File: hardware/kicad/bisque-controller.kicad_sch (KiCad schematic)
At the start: 66 parts, among them J1 USB-C, J2 5V_IN, J3 TC1_K, J4 SSR, J5 DISPLAY, J6 NAV_SW, J7 AUX, J8 TC2_K, Q1 AO3400A, Q2 AO3400A, SW1 RESET, SW2 BOOT, U1 ESP32-S3-WROOM-1U-N16R2, U2 AMS1117-3.3, U3 MAX31856MUD+, U4 USBLC6-2SC6, U5 MAX31856MUD+

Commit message: feat(hw): opto-isolate both SSR channels
LTV-817S-TA1-C per channel, indicator LED as a parallel branch (series
would not fit under 3.3V). Both opto and indicator cathodes land on
SSR_EN so the watchdog (task 12) gates the indicator too, never GND
directly. GND pour keepout across the barrier, checked by
check_isolation.py.

Footprint: Package_DIP:SMDIP-4_W9.53mm, not the brief's SO-4_4.4x4.3mm -
REV-B-NOTES.md SS7b measured all four SO-4_4.4x* candidates at a 6.0-6.3mm
pad span against the LTV-817S's ~10.16mm gull-wing lead span; any of them
would land 1.85mm/side inboard of the actual leads. Not using the
_Clearance8mm variant either: that creepage is a mains-crossing
provision, and this barrier is low-voltage on both sides.

Renumbered several of the brief's proposed designators (R15-R19) to
R18/R19/R20/R21/R22 - the brief's originals collided with R14-R17,
already assigned to task 6's MAX31856 input filters.

Also: removed 4 stale ROUTE_ORDER entries in gen_pcb.py that referenced
deleted rev-A SSR nets (would have KeyError'd), and fixed a coincident
schematic-pin bug in gen_sch.py where a new SSR2 resistor and the buzzer
driver's R11 landed on the exact same wire endpoint, silently merging
SSR2_IND_A into the ALARM net.

Co-Authored-By: Claude Opus 5 <noreply@anthropic.com>
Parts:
- removed Q1: AO3400A, Package_TO_SOT_SMD:SOT-23, symbol Transistor_FET:AO3400A
- added J9: SSR2, TerminalBlock_Phoenix:TerminalBlock_Phoenix_MKDS-1,5-2-5.08_1x02_P5.08mm_Horizontal, symbol Connector:Screw_Terminal_01x02
- added LED4: amber, LED_SMD:LED_0805_2012Metric, symbol Device:LED
- added R18, R22: 0R, Resistor_SMD:R_0805_2012Metric, symbol Device:R
- added R19: 220R, Resistor_SMD:R_0805_2012Metric, symbol Device:R
- added R20: 10k, Resistor_SMD:R_0805_2012Metric, symbol Device:R
- added R21: 680R, Resistor_SMD:R_0805_2012Metric, symbol Device:R
- added U8, U9: LTV-817S-TA1-C, Package_DIP:SMDIP-4_W9.53mm, symbol Isolator:LTV-817
- J4: value SSR -> SSR1
- R6: value 100R -> 220R
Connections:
- net SSR_CTRL is gone; now on net SSR1_CTRL: R6.1
- net +5V: no longer J4.1 (Pin_1), LED3.2 (A)
- net GND: now also R20.2
- net SSR1_CTRL: now also R10.1, R7.1
- net SSR2_CTRL: now also R19.1, R20.1, R21.1
- net LEDS_K renamed SSR1_IND_A
- net SSR1_IND_A: now also LED3.2 (A); no longer LED3.1 (K)
- net SSR_GATE renamed SSR1_LED_A
- net SSR1_LED_A: now also U8.1; no longer R7.1
- net SSR_OUT renamed SSR1_B
- net SSR1_B: now also U8.3; no longer R10.1
- new net SSR1_A: J4.1 (Pin_1), U8.4
- new net SSR1_IND_K: LED3.1 (K), R18.1
- new net SSR2_A: J9.1 (Pin_1), U9.4
- new net SSR2_B: J9.2 (Pin_2), U9.3
- new net SSR2_IND_A: LED4.2 (A), R21.2
- new net SSR2_IND_K: LED4.1 (K), R22.1
- new net SSR2_LED_A: R19.2, U9.1
- new net SSR_EN: R18.2, R22.2, U8.2, U9.2
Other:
- note added: "Bisque kiln controller - ESP32-S3-WROOM-1 SSR terminals J4/J9: opto-isolated (LTV-817S), boot-safe (R7/R20 pulldown). SSR1_A/B, SSR2_A/B float - no GND/+3V3/+5V on the isolated side. SSR_EN is the shared opto+indicator cathode return, gated by the watchdog. TC1 terminal J3 / TC2 terminal J8: pin1 = K+, pin2 = K- - both float, biased near AGND only through each MAX31856's internal BIAS network. Un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"
- note added: "SSR DRIVE x2 (opto-isolated, LTV-817S; indicator LED parallel branch)"
- note removed: "Bisque kiln controller - ESP32-S3-WROOM-1 SSR terminal J4: +5V / SSR- loop, switched low-side by Q1 (boot-safe: R7 pulldown) TC1 terminal J3 / TC2 terminal J8: pin1 = K+, pin2 = K- - both float, biased near AGND only through each MAX31856's internal BIAS network. Ungrounded-junction probes required: two grounded-junction probes in one kiln would loop through it. Nav switch J6 is panel-mounted; in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"
- note removed: "SSR DRIVE (low-side switch, J4 supplies the +5V loop)"
- moved on the sheet: J4, LED3, R10, R6, R7

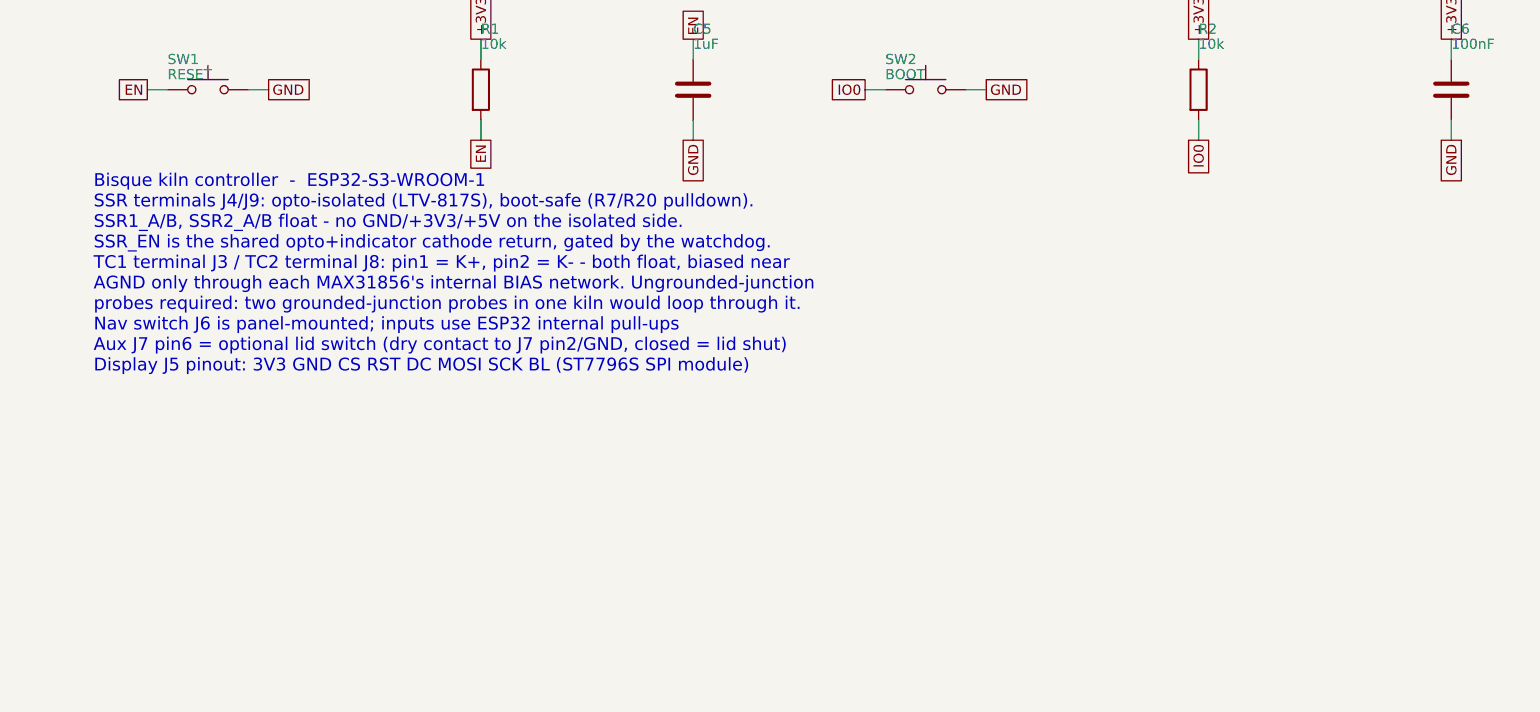
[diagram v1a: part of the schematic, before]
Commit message: feat(hw): ULN2003 aux bank with external coil rail
Vent, purge and spare on one Basic part with integrated flyback diodes.
COM lands on its own AUX_VP terminal so 12/24V solenoids work; SJ1 links
it to +5V for 5V relays.

Uses R23-R25 for the input pulldowns rather than the R20-R22 the task
brief specified: Task 7 (SSR optocoupler channels) already claimed
R20-R22, confirmed against the live design.py before adding these.

Co-Authored-By: Claude Opus 5 <noreply@anthropic.com>
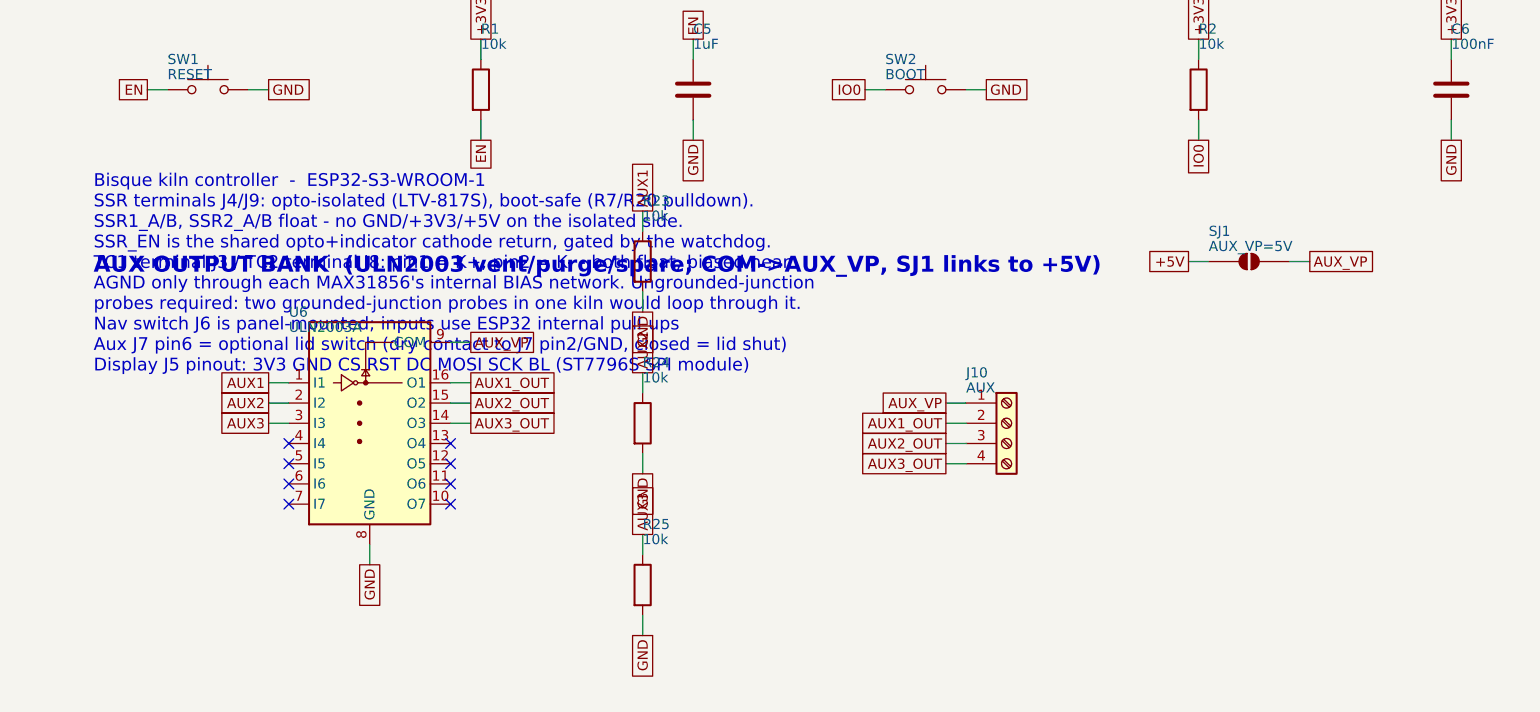
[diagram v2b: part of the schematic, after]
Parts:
- added J10: AUX, TerminalBlock_Phoenix:TerminalBlock_Phoenix_MKDS-1,5-4-5.08_1x04_P5.08mm_Horizontal, symbol Connector:Screw_Terminal_01x04
- added R23, R24, R25: 10k, Resistor_SMD:R_0805_2012Metric, symbol Device:R
- added SJ1: AUX_VP=5V, Jumper:SolderJumper-2_P1.3mm_Open_RoundedPad1.0x1.5mm, symbol Jumper:SolderJumper_2_Open
- added U6: ULN2003A, Package_SO:SOIC-16_3.9x9.9mm_P1.27mm, symbol Transistor_Array:ULN2003A
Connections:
- net +5V: now also SJ1.1 (A)
- net AUX1: now also R23.1, U6.1 (I1)
- net AUX2: now also R24.1, U6.2 (I2)
- net AUX3: now also R25.1, U6.3 (I3)
- net GND: now also R23.2, R24.2, R25.2, U6.8 (GND)
- new net AUX1_OUT: J10.2 (Pin_2), U6.16 (O1)
- new net AUX2_OUT: J10.3 (Pin_3), U6.15 (O2)
- new net AUX3_OUT: J10.4 (Pin_4), U6.14 (O3)
- new net AUX_VP: J10.1 (Pin_1), SJ1.2 (B), U6.9 (COM)
- no-connect marks 11 -> 19
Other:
- note added: "AUX OUTPUT BANK (ULN2003 vent/purge/spare; COM->AUX_VP, SJ1 links to +5V)"
